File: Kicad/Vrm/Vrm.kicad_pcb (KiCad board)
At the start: 2 copper layers, 94 x 100.3 mm, 34 parts, among them Q1 2N3704, U1 STM32F091RCTx

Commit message: Added minor changes from manlab
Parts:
- removed the REF** at (218.4, 58.4)
- removed the REF** at (132.1, 149.9)
- removed the REF** at (132.1, 58.4)
- removed the REF** at (246.4, 96.5)
- removed the REF** at (218.4, 149.9)
- added REF**: SOT-23, Package_TO_SOT_SMD:SOT-23, F.Cu at (132.1, 86.4)
- added REF**: LT1302, Package_SO:SOIC-8-1EP_3.9x4.9mm_P1.27mm_EP2.29x3mm, F.Cu at (198.1, 38.1)
- added REF**: MountingHole_3.5mm, MountingHole:MountingHole_3.5mm, F.Cu at (215.9, 61.0)
- added REF**: MountingHole_3.5mm, MountingHole:MountingHole_3.5mm, F.Cu at (134.6, 147.3)
- added REF**: MountingHole_3.5mm, MountingHole:MountingHole_3.5mm, F.Cu at (215.9, 147.3)
- added REF**: LTC3631, Package_SO:MSOP-8_3x3mm_P0.65mm, F.Cu at (175.3, 38.1)
- added REF**: MountingHole_3.5mm, MountingHole:MountingHole_3.5mm, F.Cu at (134.6, 61.0)
- moved REF** 8.03 mm to (147.3, 61.0)
- moved REF** 8.03 mm to (163.8, 61.0)
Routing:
- net GND: track 348.0 -> 356.7 mm
- net VDD: track 185.6 -> 191.3 mm

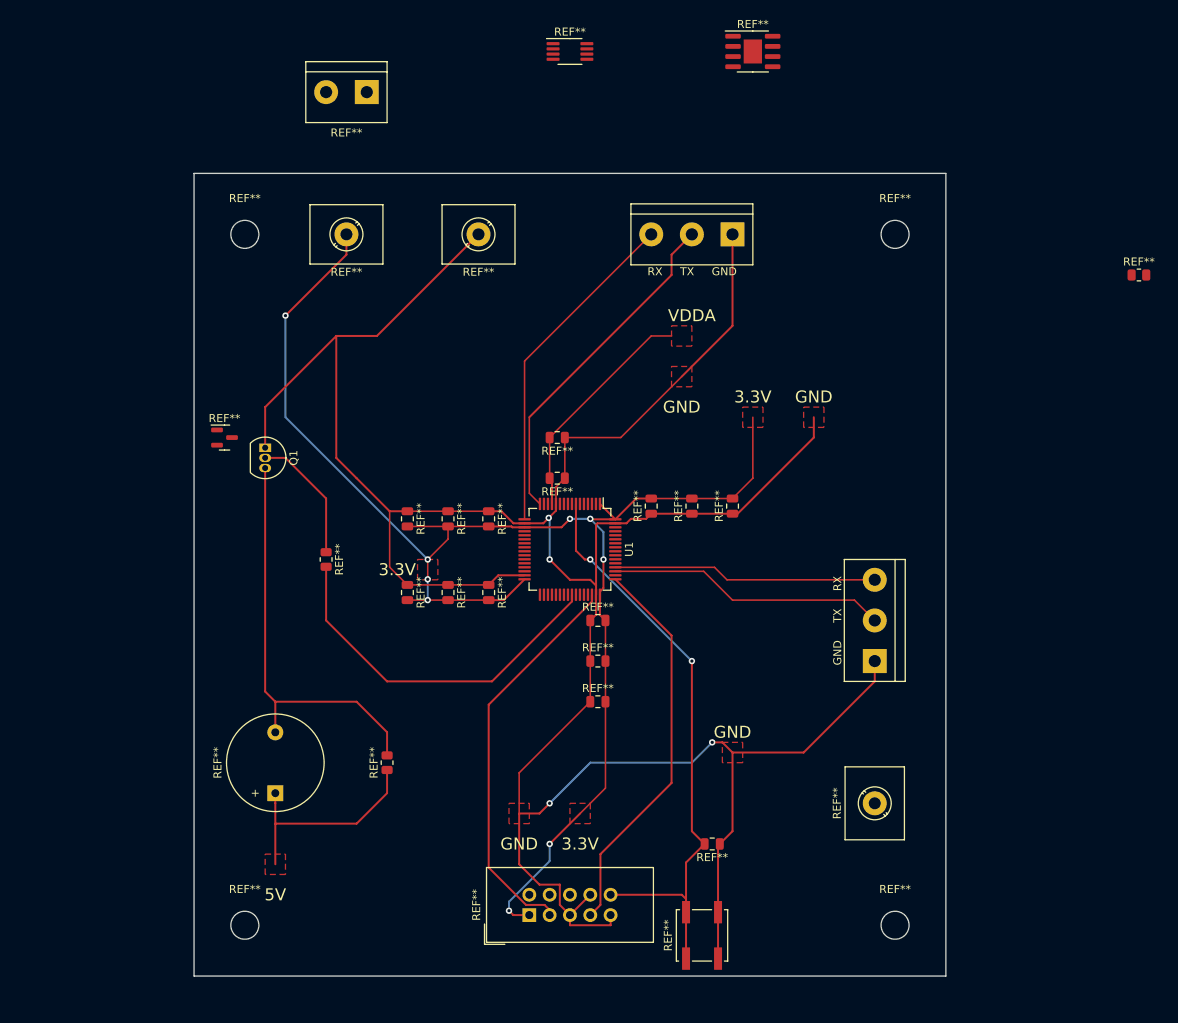
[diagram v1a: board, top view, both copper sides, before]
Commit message: Power/GND beef up
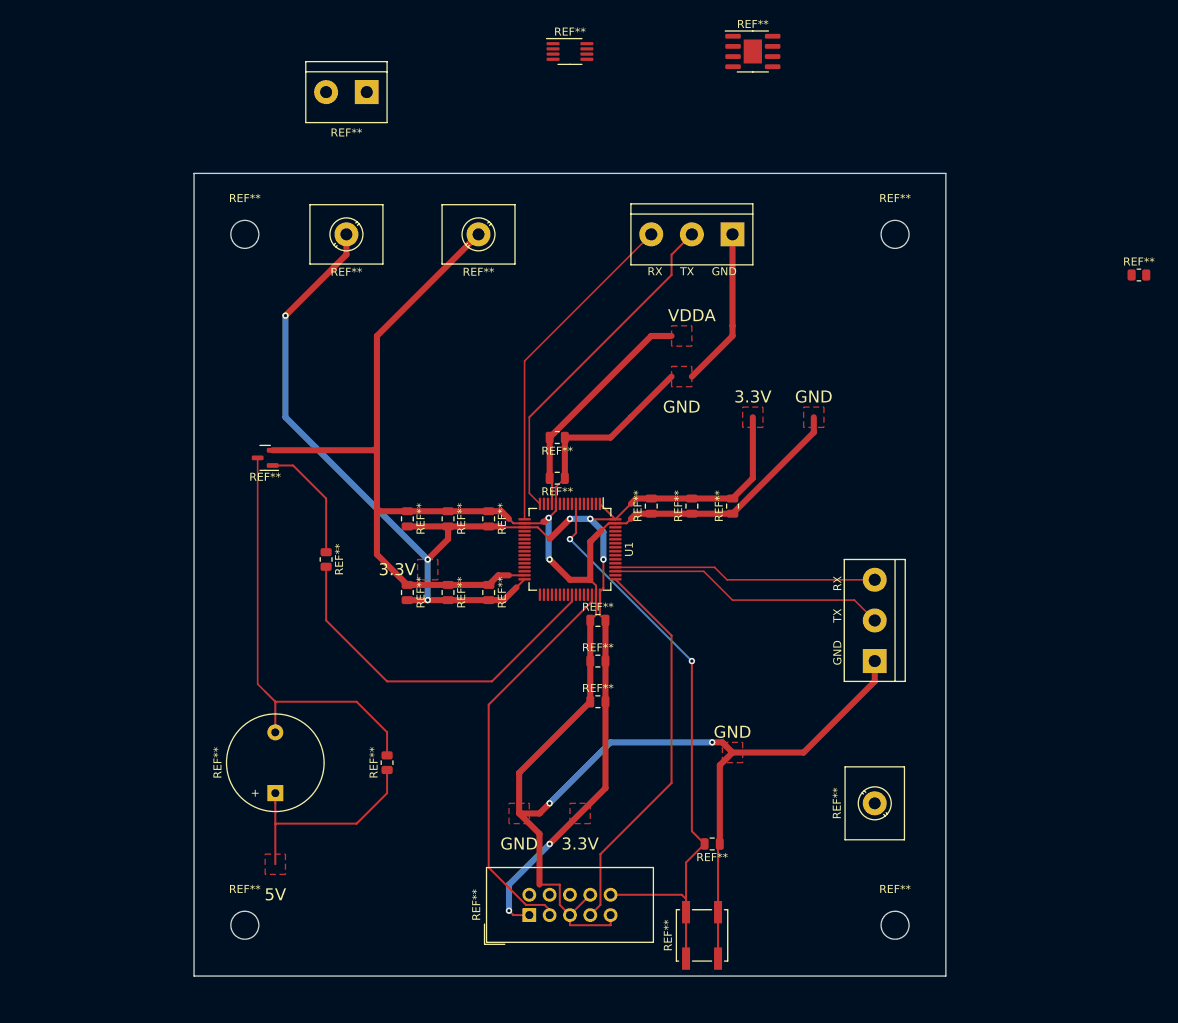
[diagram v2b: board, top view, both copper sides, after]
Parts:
- removed Q1: 2N3704, Package_TO_SOT_THT:TO-92_Inline
- moved REF** 5.68 mm to (137.2, 88.9), turned to 180 degrees
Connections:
- REF** pad 1: (no net) -> unconnected-(Q1-Pad2)
- REF** pad 2: (no net) -> GND
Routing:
- net GND: track 356.7 -> 343.2 mm
- net (no net): track 232.2 -> 233.9 mm
- net unconnected-(Q1-Pad2): track 16.4 -> 15.1 mm
- net VDD: track 191.3 -> 192.4 mm, vias 9 -> 8

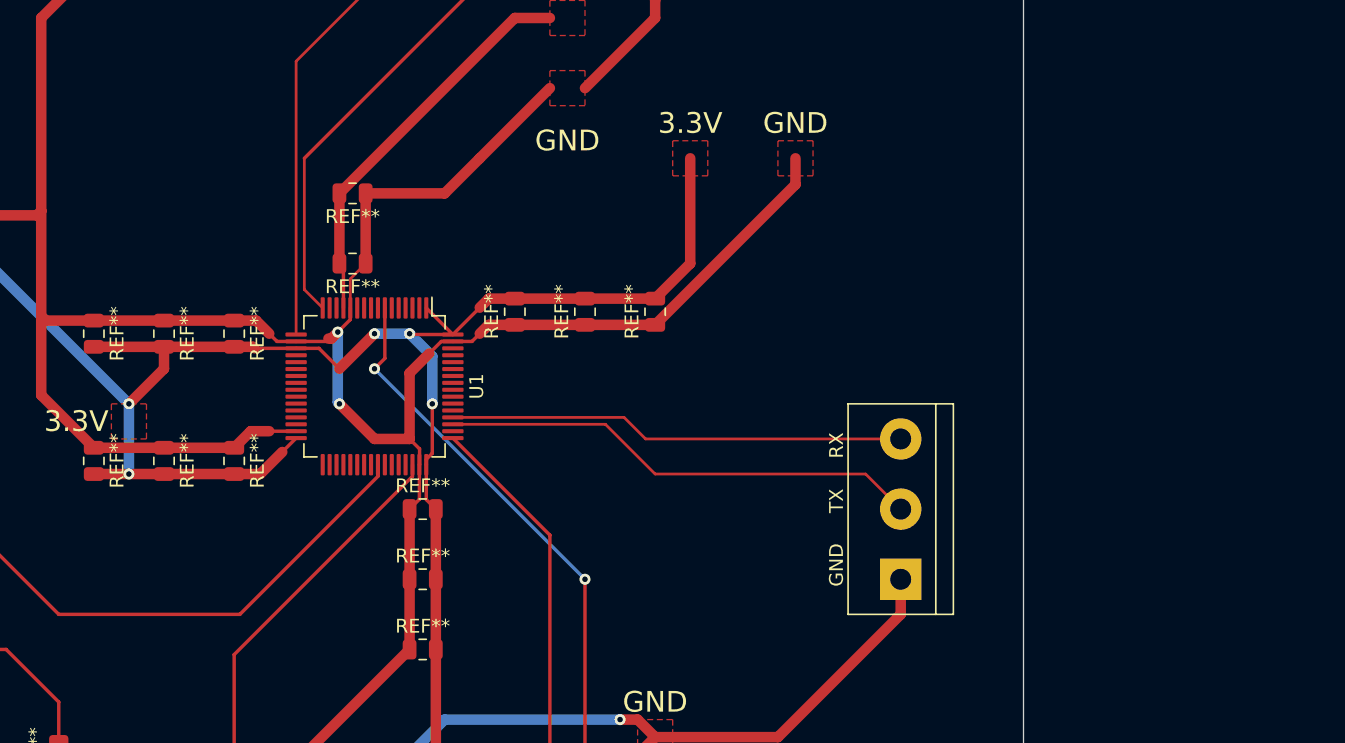
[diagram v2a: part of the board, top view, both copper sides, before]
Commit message: Pushed in decoupling caps
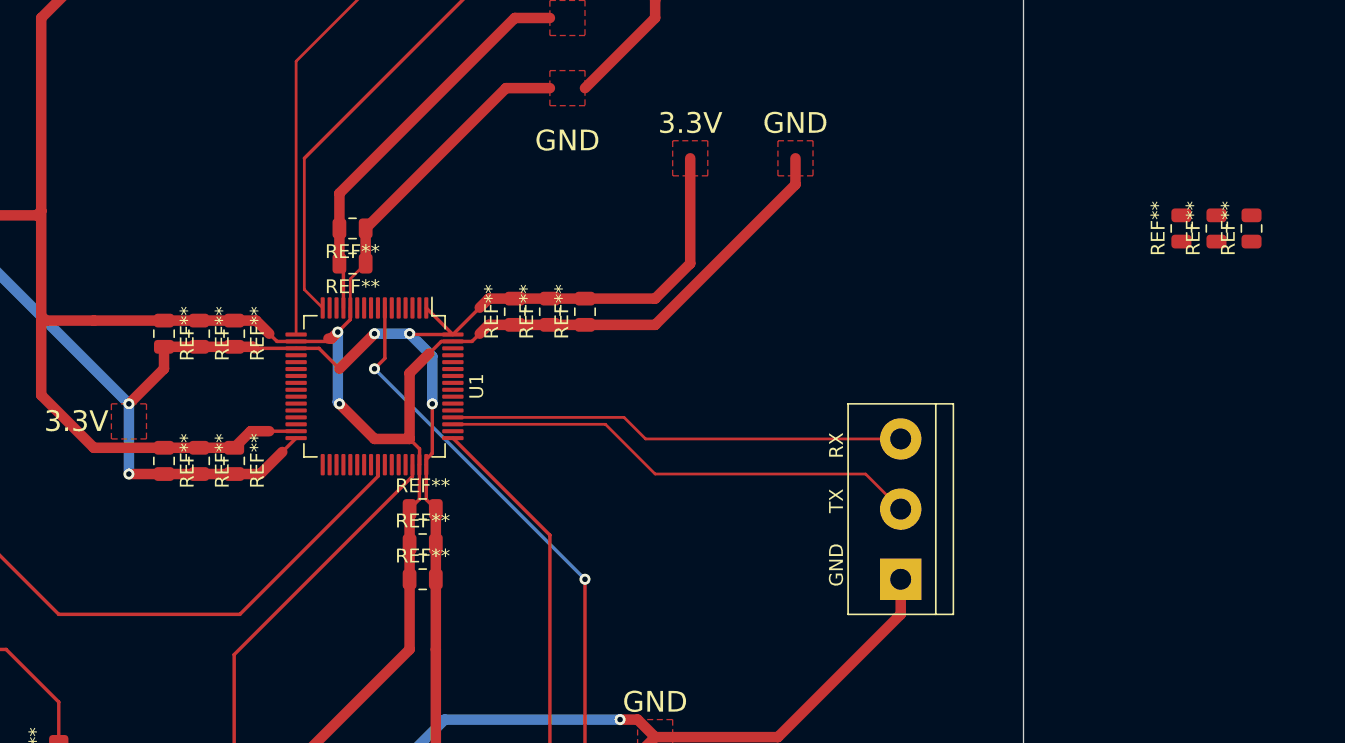
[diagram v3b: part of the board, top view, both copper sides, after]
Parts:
- added REF**: 100nF, Capacitor_SMD:C_0805_2012Metric, F.Cu at (236.2, 88.9)
- added REF**: 100nF, Capacitor_SMD:C_0805_2012Metric, F.Cu at (238.8, 88.9)
- added REF**: 100nF, Capacitor_SMD:C_0805_2012Metric, F.Cu at (233.7, 88.9)
- moved REF** 5.08 mm to (160.0, 105.7)
- moved REF** 5.08 mm to (190.5, 94.9)
- moved REF** 5.08 mm to (160.0, 96.5)
- moved REF** 5.08 mm to (178.8, 114.3)
- moved REF** 2.54 mm to (173.7, 88.9)
- moved REF** 2.54 mm to (162.6, 96.5)
- moved REF** 2.54 mm to (162.6, 105.7)
- moved REF** 2.54 mm to (188.0, 94.9)
- moved REF** 2.54 mm to (178.8, 111.8)
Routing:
- net VDD: track 192.4 -> 184.8 mm
- net GND: track 343.2 -> 341.7 mm

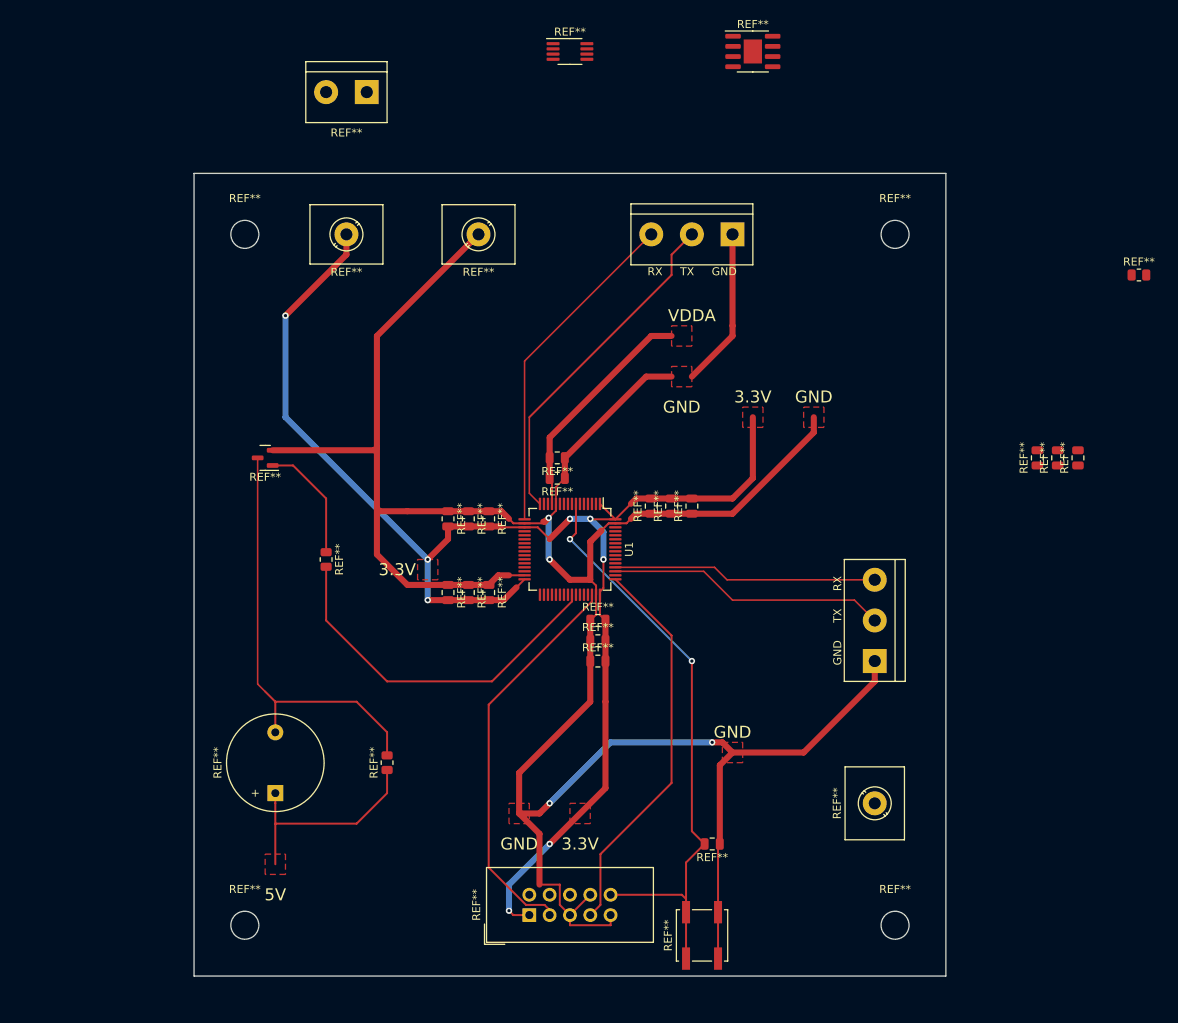
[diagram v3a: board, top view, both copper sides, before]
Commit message: Added UART resistors, new buzzer, UART breakout, and ground plane
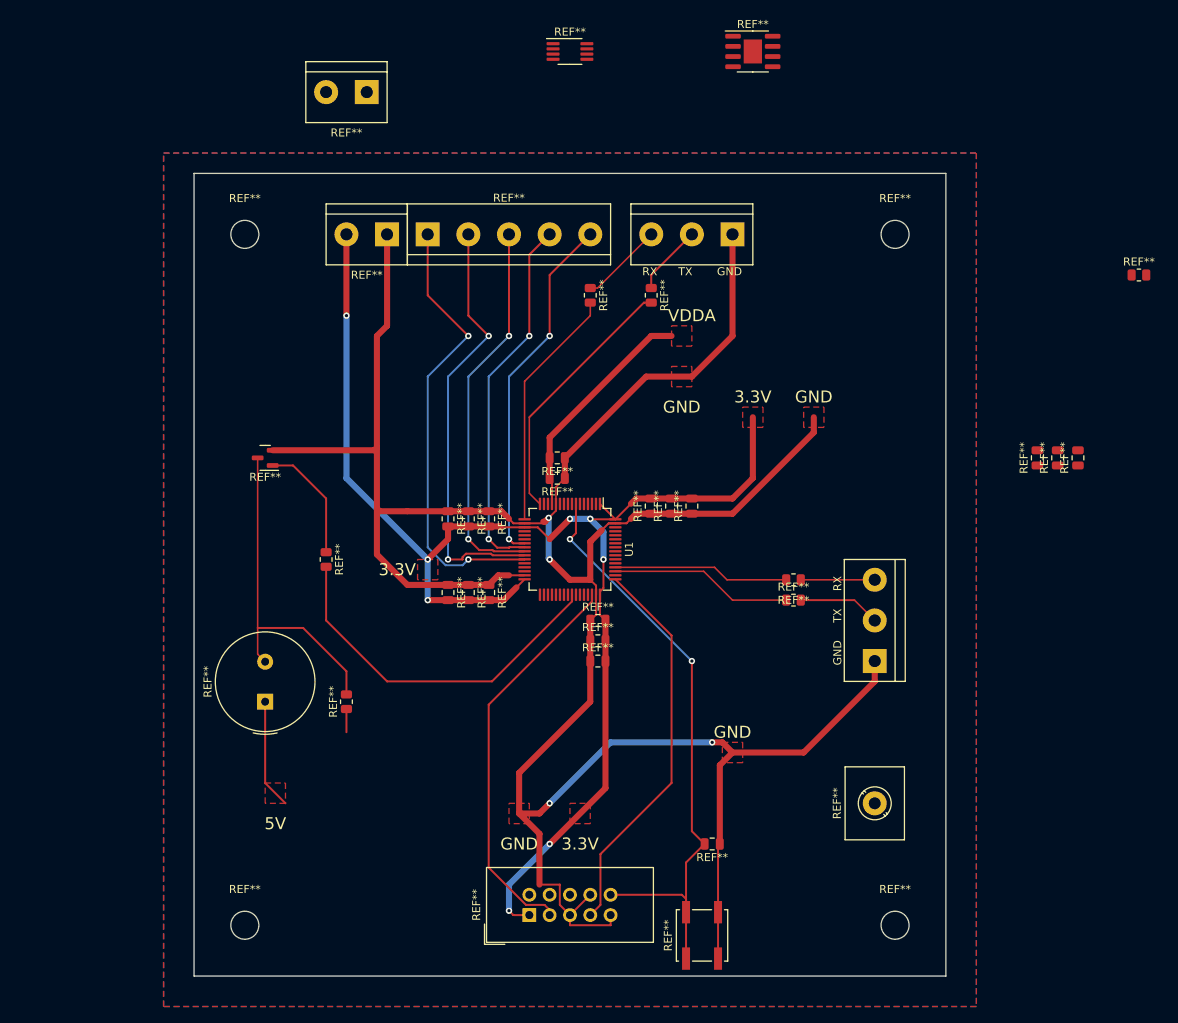
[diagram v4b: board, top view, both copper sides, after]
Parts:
- removed the REF** at (147.3, 61.0)
- removed the REF** at (138.4, 130.8)
- removed the REF** at (163.8, 61.0)
- added REF**: Buzzer, Buzzer_Beeper:Buzzer_TDK_PS1240P02BT_D12.2mm_H6.5mm, F.Cu at (137.2, 119.4)
- added REF**: GPIO 5-1, TerminalBlock:TerminalBlock_bornier-5_P5.08mm, F.Cu at (157.5, 61.0)
- added REF**: VDD GND, TerminalBlock:TerminalBlock_bornier-2_P5.08mm, F.Cu at (152.4, 61.0)
- added REF**: R4 (25), Resistor_SMD:R_0805_2012Metric, F.Cu at (203.2, 106.7)
- added REF**: R3 (25), Resistor_SMD:R_0805_2012Metric, F.Cu at (203.2, 104.1)
- added REF**: R5 (25), Resistor_SMD:R_0805_2012Metric, F.Cu at (177.8, 68.6)
- added REF**: R6 (25), Resistor_SMD:R_0805_2012Metric, F.Cu at (185.4, 68.6)
-    RX      TX       GND: renamed from RX     TX     GND
- moved REF** 9.16 mm to (147.3, 119.4)
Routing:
- net unconnected-(U1-Pad27): track 0.00 -> 56.7 mm, vias 0 -> 2
- net unconnected-(U1-Pad26): track 0.00 -> 53.9 mm, vias 0 -> 2
- net unconnected-(U1-Pad25): track 0.00 -> 47.9 mm, vias 0 -> 2
- net unconnected-(U1-Pad24): track 0.00 -> 46.2 mm, vias 0 -> 2
- net unconnected-(U1-Pad23): track 0.00 -> 44.5 mm, vias 0 -> 2
- net (no net): track 233.9 -> 205.4 mm
- net VDD: track 184.8 -> 178.5 mm
- net GND: track 341.7 -> 339.5 mm
- added copper zone on B.Cu, net VDD

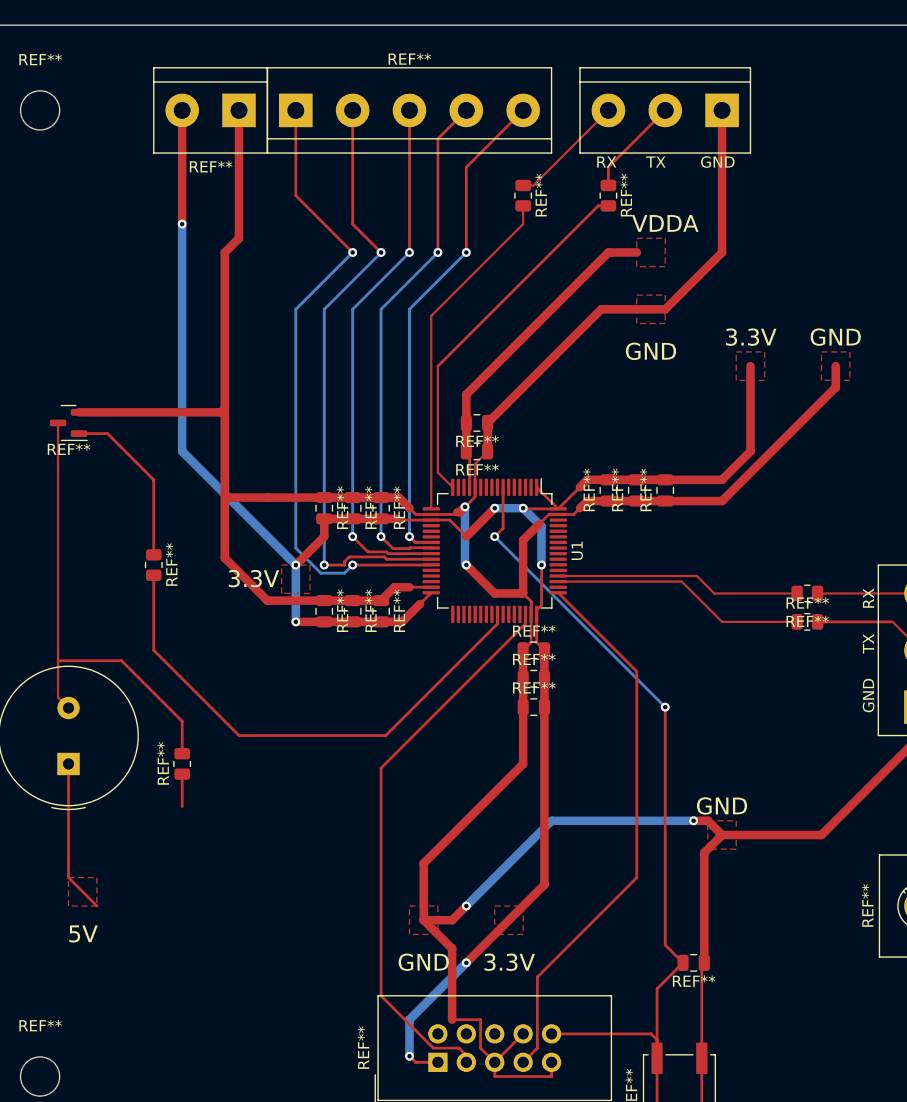
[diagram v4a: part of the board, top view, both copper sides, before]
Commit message: Added PUPD resistors, ground plane
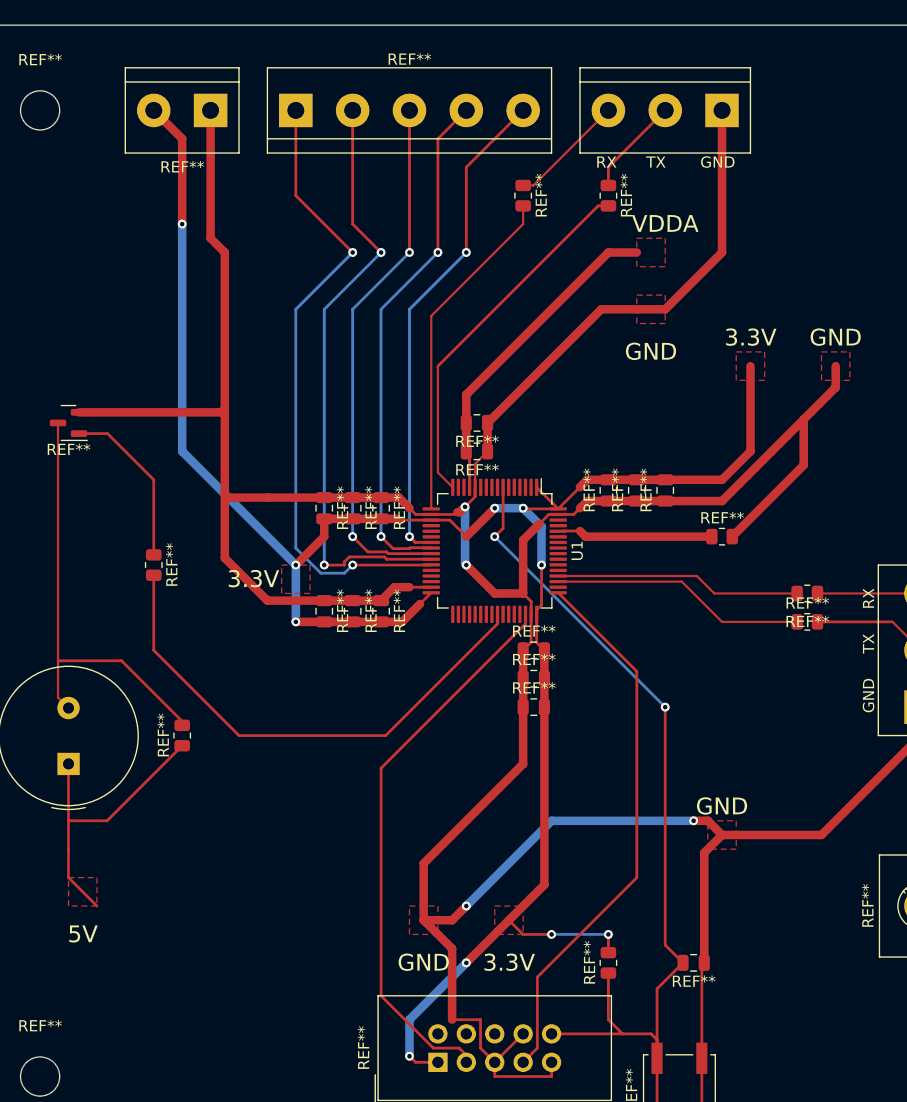
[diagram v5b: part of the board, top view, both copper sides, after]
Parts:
- added REF**: R7 (10k), Resistor_SMD:R_0805_2012Metric, F.Cu at (195.6, 99.1)
- added REF**: R8 (10k), Resistor_SMD:R_0805_2012Metric, F.Cu at (185.4, 137.2)
- moved REF** 2.54 mm to (149.9, 61.0)
- moved REF** 2.54 mm to (147.3, 116.8)
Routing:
- net unconnected-(U1-Pad60): track 0.00 -> 13.5 mm
- net GND: track 339.5 -> 352.6 mm
- net VDD: track 178.5 -> 190.6 mm, vias 8 -> 10
- net (no net): track 205.4 -> 212.9 mm
- net NRST: track 76.4 -> 82.3 mm
